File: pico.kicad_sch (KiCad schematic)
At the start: 7 parts, among them J12 I2C, Q4 DMG2305UX, U14 Pico

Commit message: more cleanup and added notes for review
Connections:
- net GP21 renamed DIGITAL_GP21
- net GP22 renamed DIGITAL_GP22
- net INT renamed ~{CAN_INTERRUPT}
- net NEW_GP14 renamed DIGITAL_GP14
- net NEW_GP15 renamed DIGITAL_GP15

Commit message: major rework again after the meeting
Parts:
- added D10: BAD, LED_SMD:LED_0805_2012Metric_Pad1.15x1.40mm_HandSolder, symbol Device:LED
- added D9: GOOD, LED_SMD:LED_0805_2012Metric_Pad1.15x1.40mm_HandSolder, symbol Device:LED
- added J3: UART, Connector_Molex:Molex_PicoBlade_53047-0410_1x04_P1.25mm_Vertical, symbol Connector_Generic:Conn_01x04
- added Q5, Q6: Q_NMOS, Package_TO_SOT_SMD:TSOT-23, symbol Transistor_FET:Q_NMOS_DGS
- added R1, R5: 511, Resistor_SMD:R_0805_2012Metric_Pad1.20x1.40mm_HandSolder, symbol Device:R_US
- added TP12: LED1, TestPoint:TestPoint_Pad_D1.0mm, symbol Connector:TestPoint
- added TP13: LED2, TestPoint:TestPoint_Pad_D1.0mm, symbol Connector:TestPoint
- C20: footprint Payload_PCB_v3.1:UCM1H220MCL1GS -> Capacitor_SMD:C_Elec_4x5.4
- U14: value Pico -> PI_PICO
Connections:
- net +3.3V: now also J3.1 (Pin_1), R1.2, R5.2; no longer Q4.3 (D)
- net GND: now also J3.4 (Pin_4), Q5.3 (S), Q6.3 (S)
- net I2C0_SCL: now also J12.3 (Pin_3); no longer J12.2 (Pin_2)
- net I2C0_SDA: now also J12.2 (Pin_2); no longer J12.3 (Pin_3)
- net ANALOG_POT3 renamed ANALOG_MANIPULATOR
- net DIGITAL_GP14 renamed DIGITAL_LIMIT_SW1
- net DIGITAL_GP15 renamed DIGITAL_LIMIT_SW2
- net DIGITAL_GP21 renamed DIGITAL_RELAY1
- net DIGITAL_GP22 renamed DIGITAL_RELAY2
- net LED1 renamed LED_GOOD
- net LED_GOOD: now also Q5.2 (G), TP12.1
- net LED2 renamed LED_BAD
- net LED_BAD: now also Q6.2 (G), TP13.1
- net LED3 renamed UART0_TX
- net LED4 renamed UART0_RX
- net SERVO5_PICO: no longer names the net of U14.9 (GPIO6)
- net SERVO6_PICO: no longer names the net of U14.10 (GPIO7)
- net SERVO7_PICO renamed UART1_TX
- net UART1_TX: now also J3.2 (Pin_2)
- net SERVO8_PICO renamed UART1_RX
- net UART1_RX: now also J3.3 (Pin_3)
- new net: D9.1 (K), Q5.1 (D)
- new net: D9.2 (A), R1.1
- new net: D10.1 (K), Q6.1 (D)
- new net: D10.2 (A), R5.1
- new net +5V: Q4.3 (D)
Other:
- note added: "DEBUG PORTS"
- note added: "PROTECTION"
- note added: "STATUS LEDs"
- note removed: "RASPBERRY PI PICO MICROCONTROLLER"
- moved on the sheet: C20, C22, J12, Q4, R22, R23, U14

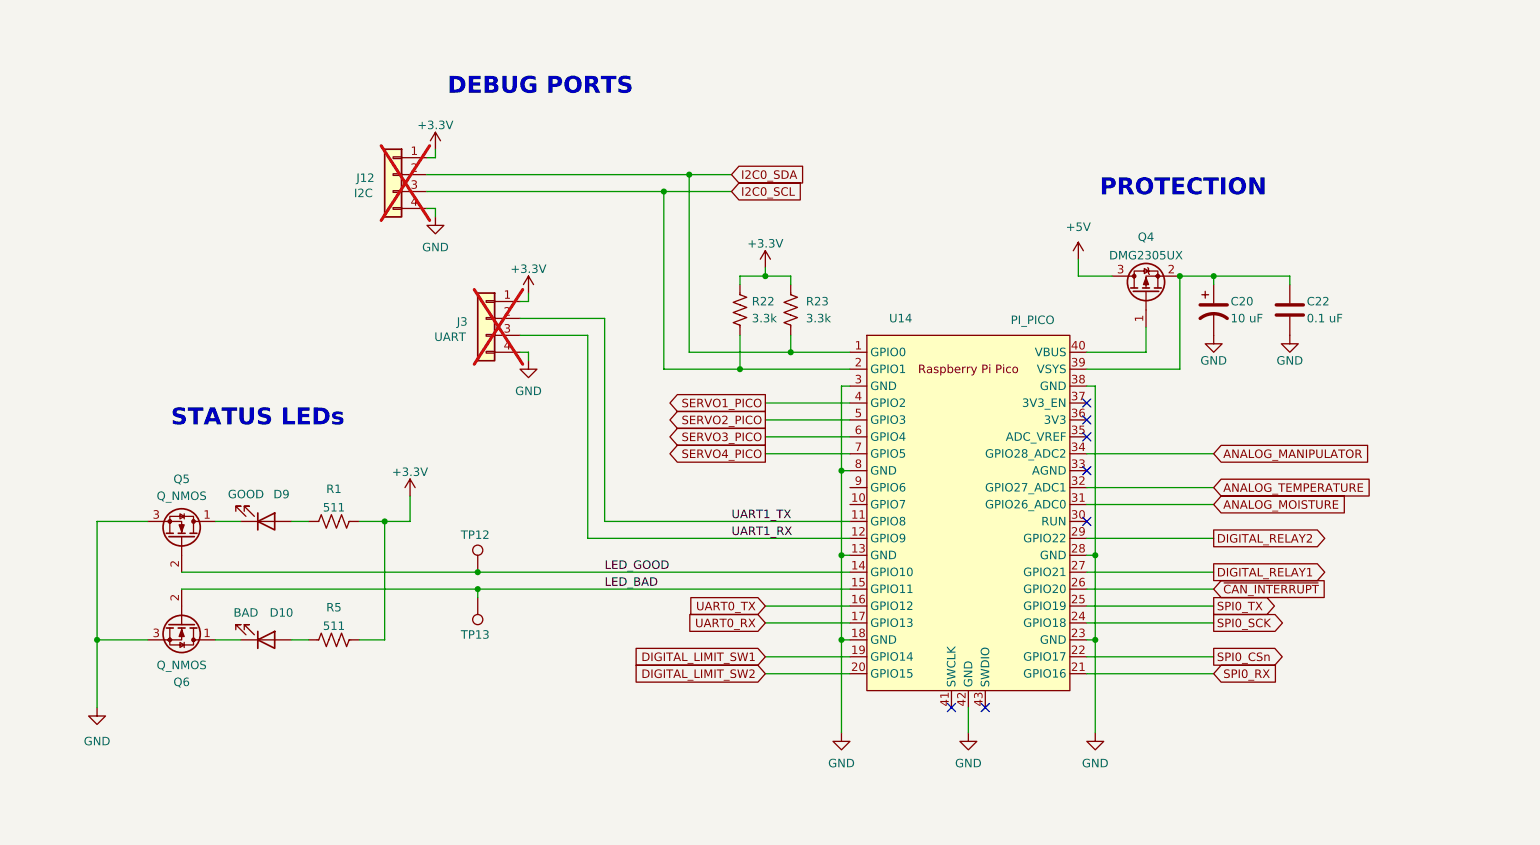
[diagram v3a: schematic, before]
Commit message: major finishing touches:     - major rework for v5.1     - silkscreen and stuff     - impednace for USB and CAN lines     - schematic comments     - symbol, footprint, and model library updates
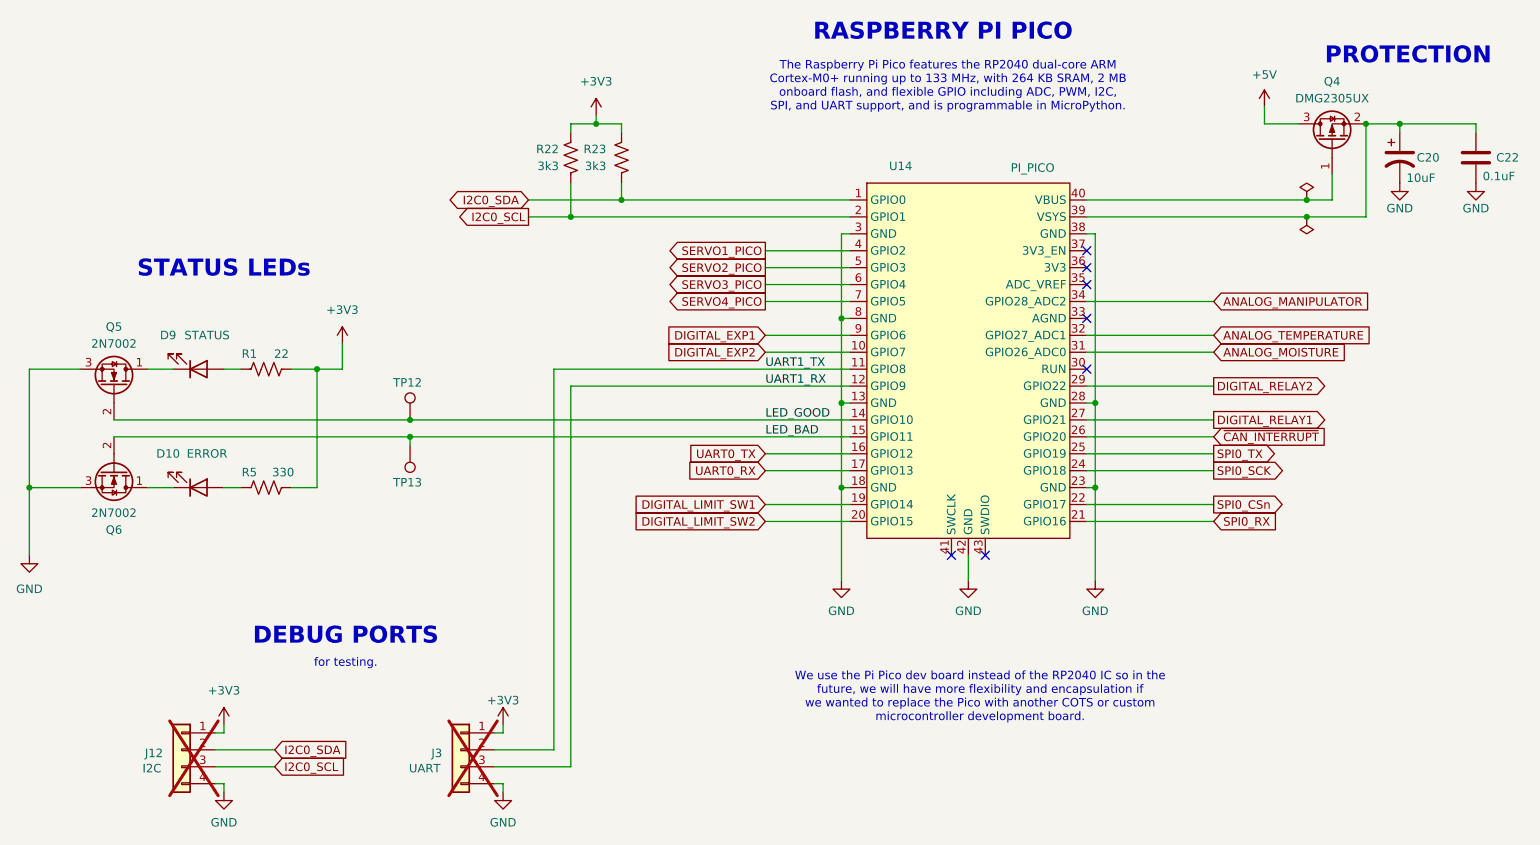
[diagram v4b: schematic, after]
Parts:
- C20: value 10 uF -> 10uF; footprint Capacitor_SMD:C_Elec_4x5.4 -> Capacitor_THT:CP_Radial_D8.0mm_P2.50mm; Manufacturer (none) -> Nichicon; Manufacturer Part Number (none) -> UVR2C100MPD1TD; Vendor (none) -> Digikey; Vendor Part Number (none) -> 493-12828-1-ND
- C22: value 0.1 uF -> 0.1uF; Manufacturer (none) -> KEMET; Manufacturer Part Number (none) -> C1206C104J5RACTU; Vendor (none) -> Digikey; Vendor Part Number (none) -> 399-C1206C104J5RACTUCT-ND
- D10: value BAD -> ERROR; Manufacturer (none) -> Würth Elektronik; Manufacturer Part Number (none) -> 150080RS75000; Vendor (none) -> Digikey; Vendor Part Number (none) -> 732-4984-1-ND
- D9: value GOOD -> STATUS; Manufacturer (none) -> Würth Elektronik; Manufacturer Part Number (none) -> 150080BS75000; Vendor (none) -> Digikey; Vendor Part Number (none) -> 732-4982-1-ND
- J12, J3: Manufacturer (none) -> Molex; Manufacturer Part Number (none) -> 0530470410; Vendor (none) -> Digikey; Vendor Part Number (none) -> WM1733-ND
- Q4: symbol Device:Q_PMOS_GSD -> Transistor_FET:Q_PMOS_GSD; Manufacturer (none) -> Diodes Incorporated; Manufacturer Part Number (none) -> DMG2305UX-7; Vendor (none) -> Digikey; Vendor Part Number (none) -> DMG2305UX-7DICT-ND
- Q5, Q6: value Q_NMOS -> 2N7002; Manufacturer (none) -> onsemi; Manufacturer Part Number (none) -> 2N7002; Vendor (none) -> Digikey; Vendor Part Number (none) -> 2N7002NCT-ND
- R1: value 511 -> 22; footprint Resistor_SMD:R_0805_2012Metric_Pad1.20x1.40mm_HandSolder -> Resistor_SMD:R_0603_1608Metric_Pad0.98x0.95mm_HandSolder; Manufacturer (none) -> Stackpole Electronics Inc; Manufacturer Part Number (none) -> RNCP0603FTD22R1; Vendor (none) -> Digikey; Vendor Part Number (none) -> RNCP0603FTD22R1CT-ND
- R22, R23: value 3.3k -> 3k3; footprint Resistor_SMD:R_0805_2012Metric_Pad1.20x1.40mm_HandSolder -> Resistor_SMD:R_0603_1608Metric_Pad0.98x0.95mm_HandSolder; Manufacturer (none) -> Stackpole Electronics Inc; Manufacturer Part Number (none) -> RNCP0603FTD3K30; Vendor (none) -> Digikey; Vendor Part Number (none) -> 738-RNCP0603FTD3K30CT-ND
- R5: value 511 -> 330; footprint Resistor_SMD:R_0805_2012Metric_Pad1.20x1.40mm_HandSolder -> Resistor_SMD:R_0603_1608Metric_Pad0.98x0.95mm_HandSolder; Manufacturer (none) -> Stackpole Electronics Inc; Manufacturer Part Number (none) -> RNCP0603FTD332R; Vendor (none) -> Digikey; Vendor Part Number (none) -> RNCP0603FTD332RCT-ND
- TP12, TP13: now left out of the parts list
- U14: symbol MCU_RaspberryPi_and_Boards:Pico -> symbols:RPi_Pico; Manufacturer (none) -> Raspberry Pi; Manufacturer Part Number (none) -> SC0915; Vendor (none) -> Digikey; Vendor Part Number (none) -> 2648-SC0915TR-ND
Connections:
- net DIGITAL_EXP2: now reaches U14.10 (GPIO7)
- net DIGITAL_EXP1: now reaches U14.9 (GPIO6)
- net at D10.2 (A): now also R5.2; no longer R5.1
- net +3.3V renamed +3V3
- net +3V3: now also R5.1; no longer R5.2
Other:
- note added: "RASPBERRY PI PICO"
- note added: "The Raspberry Pi Pico features the RP2040 dual-core ARM Cortex-M0+ running up to 133 MHz, with 264 KB SRAM, 2 MB onboard flash, and flexible GPIO including ADC, PWM, I2C, SPI, and UART support, and is programmable in MicroPython."
- note added: "We use the Pi Pico dev board instead of the RP2040 IC so in the future, we will have more flexibility and encapsulation if we wanted to replace the Pico with another COTS or custom microcontroller development board."
- note added: "for testing."
- company: WVU Unviersity Rover Challenge -> WVU Unviersity Rover Challenge (URC)
- moved on the sheet: C20, C22, D10, D9, J12, J3, Q4, Q5, Q6, R22, R23, TP12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

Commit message: some repo cleanup
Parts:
- U14: Notes (none) -> The Raspberry Pi Pico features the RP2040 dual-core ARM Cor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
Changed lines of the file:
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@@
 			)
 		)
-		(property "Notes" ""
+		(property "Notes" "The Raspberry Pi Pico features the RP2040 dual-core ARM Cortex-M0+ running up to 133 MHz, with 264 KB SRAM, 2 MB onboard flash, and flexible GPIO including ADC, PWM, I2C, SPI, and UART support, and is programmable in MicroPython."
 			(at 177.8 83.82 0)
 			(effects
-				(font
-					(size 1.27 1.27)
-				)
-				(hide yes)
-			)
-		)
-		(property "KLC_S4.2_3V3OUT" ""
-			(at 177.8 83.82 0)
-			(effects
-				(font
-					(size 1.27 1.27)
-				)
-				(hide yes)
-			)
-		)
-		(property "KLC_S4.2_VCC" ""
-			(at 177.8 83.82 0)
-			(effects

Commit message: some more docs. updated pico VPN to CT
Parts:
- U14: Vendor Part Number 2648-SC0915TR-ND -> 2648-SC0915CT-ND

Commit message: swapped UART to USB from FTDI (out of stock) to MCP2200
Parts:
- U14: footprint MCU_RaspberryPi_and_Boards:RPi_Pico_SMD_TH -> footprints:RPi_Pico_SMD_TH
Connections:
- net LED_BAD renamed LED_ERROR
- net LED_GOOD renamed LED_STATUS
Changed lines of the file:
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@@
 		)
 	)
-	(label "LED_BAD"
-		(at 147.32 95.25 0)
+	(label "LED_ERROR"
+		(at 121.92 95.25 0)
 		(effects
 			(font
@@
 	)
 	(label "UART1_TX"
-		(at 147.32 85.09 0)
+		(at 121.92 85.09 0)
 		(effects
 			(font
@@
 	)
 	(label "UART1_RX"
-		(at 147.32 87.63 0)
+		(at 121.92 87.63 0)
 		(effects
 			(font
@@
 		)
 	)
-	(label "LED_GOOD"
-		(at 147.32 92.71 0)
+	(label "LED_STATUS"
+		(at 121.92 92.71 0)
 		(effects
 			(font
@@
 	)
 	(global_label "UART0_TX"
-		(shape input)
+		(shape output)
 		(at 147.32 97.79 180)
 		(fields_autoplaced yes)
@@
 			)
 		)
-		(property "Footprint" "MCU_RaspberryPi_and_Boards:RPi_Pico_SMD_TH"
+		(property "Footprint" "footprints:RPi_Pico_SMD_TH"
 			(at 177.8 83.82 90)
 			(effects

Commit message: added release documents for v5.1 (pending approval)
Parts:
- D10, D9: Manufacturer Würth Elektronik -> Wurth Elektronik
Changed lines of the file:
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@@
 			)
 		)
-		(property "Manufacturer" "Würth Elektronik"
+		(property "Manufacturer" "Wurth Elektronik"
 			(at 62.23 85.09 0)
 			(effects
@@
 			)
 		)
-		(property "Manufacturer" "Würth Elektronik"
+		(property "Manufacturer" "Wurth Elektronik"
 			(at 62.23 102.87 0)
 			(effects
